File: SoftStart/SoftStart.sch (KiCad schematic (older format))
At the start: 26 parts, among them J1 LIVE, J10 LIVE, J2 NEUTRAL, J3 SW1, J4 SW2, J5 NEUTRAL, J6 SWOUTPUT, J7 LIVE, J8 LIVE, J9 LIVE

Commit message: Submitted to JLCPCB 2020-08-24
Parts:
- C1: LCSC (none) -> C342770
- C2: LCSC (none) -> C390065
- C3: LCSC (none) -> C338226
- D1, D2, D3, D4: LCSC (none) -> C193790
- D5: LCSC (none) -> C2552
- D6: LCSC (none) -> C99771
- R1: LCSC (none) -> C334296
- R2: LCSC (none) -> C58595
- R3, R4, R5, R6: value 220R -> 150R; LCSC (none) -> C334292
- RLY1: LCSC (none) -> C133339
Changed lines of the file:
@@
 F 2 "SoftStart:SMIHRelay" H 6550 2450 60  0001 C CNN
 F 3 "" H 6550 2450 60  0001 C CNN
+F 4 "C133339" H 6550 2450 60  0001 C CNN "LCSC"
 	1    6550 2450
 	1    0    0    -1
@@
 F 2 "Capacitors_THT:C_Rect_L11.5mm_W4.5mm_P10.00mm_MKT" H 2700 2600 50  0001 C CNN
 F 3 "" H 2700 2600 50  0001 C CNN
+F 4 " C342770" H 2700 2600 60  0001 C CNN "LCSC"
 	1    2700 2600
 	0    1    1    0
@@
 F 2 "Resistors_THT:R_Axial_Power_L20.0mm_W6.4mm_P22.40mm" V 3330 2600 50  0001 C CNN
 F 3 "" H 3400 2600 50  0001 C CNN
+F 4 "C334296" V 3400 2600 60  0001 C CNN "LCSC"
 	1    3400 2600
 	0    1    1    0
@@
 F 2 "Capacitors_THT:C_Rect_L24.0mm_W10.1mm_P22.50mm_MKT" H 3800 2600 50  0001 C CNN
 F 3 "" H 3800 2600 50  0001 C CNN
+F 4 "C390065" H 3800 2600 60  0001 C CNN "LCSC"
 	1    3800 2600
 	0    1    1    0
@@
 F 2 "Diodes_THT:D_DO-41_SOD81_P7.62mm_Horizontal" H 4100 2350 50  0001 C CNN
 F 3 "" H 4100 2350 50  0001 C CNN
+F 4 "C193790" H 4100 2350 60  0001 C CNN "LCSC"
 	1    4100 2350
 	0    1    1    0
@@
 F 2 "Diodes_THT:D_DO-41_SOD81_P7.62mm_Horizontal" H 4100 2850 50  0001 C CNN
 F 3 "" H 4100 2850 50  0001 C CNN
+F 4 "C193790" H 4100 2850 60  0001 C CNN "LCSC"
 	1    4100 2850
 	0    1    1    0
@@
 F 2 "Diodes_THT:D_DO-41_SOD81_P7.62mm_Horizontal" H 4500 2350 50  0001 C CNN
 F 3 "" H 4500 2350 50  0001 C CNN
+F 4 "C193790" H 4500 2350 60  0001 C CNN "LCSC"
 	1    4500 2350
 	0    1    1    0
@@
 F 2 "Diodes_THT:D_DO-41_SOD81_P7.62mm_Horizontal" H 4500 2850 50  0001 C CNN
 F 3 "" H 4500 2850 50  0001 C CNN
+F 4 "C193790" H 4500 2850 60  0001 C CNN "LCSC"
 	1    4500 2850
 	0    1    1    0
@@
 F 2 "Diodes_THT:D_DO-41_SOD81_P7.62mm_Horizontal" H 4900 2550 50  0001 C CNN
 F 3 "" H 4900 2550 50  0001 C CNN
+F 4 "C2552" H 4900 2550 60  0001 C CNN "LCSC"
 	1    4900 2550
 	0    1    1    0
@@
 F 2 "Capacitors_THT:CP_Radial_D10.0mm_P5.00mm" H 5250 2550 50  0001 C CNN
 F 3 "" H 5250 2550 50  0001 C CNN
+F 4 "C338226" H 5250 2550 60  0001 C CNN "LCSC"
 	1    5250 2550
 	1    0    0    -1
@@
 F 2 "LEDs:LED_D3.0mm" H 5650 2850 50  0001 C CNN
 F 3 "" H 5650 2850 50  0001 C CNN
+F 4 "C99771" H 5650 2850 60  0001 C CNN "LCSC"
 	1    5650 2850
 	0    -1   -1   0
@@
 F 2 "Resistors_THT:R_Axial_DIN0207_L6.3mm_D2.5mm_P7.62mm_Horizontal" V 5580 2400 50  0001 C CNN
 F 3 "" H 5650 2400 50  0001 C CNN
+F 4 "C58595" V 5650 2400 60  0001 C CNN "LCSC"
 	1    5650 2400
 	-1   0    0    1
@@
 P 7950 2250
 F 0 "R3" V 8030 2250 50  0000 C CNN
-F 1 "220R" V 7950 2250 50  0000 C CNN
+F 1 "150R" V 7950 2250 50  0000 C CNN
 F 2 "Resistors_THT:R_Axial_Power_L20.0mm_W6.4mm_P22.40mm" V 7880 2250 50  0001 C CNN
 F 3 "" H 7950 2250 50  0001 C CNN
+F 4 "C334292" V 7950 2250 60  0001 C CNN "LCSC"
 	1    7950 2250
 	-1   0    0    1
@@
 P 8350 2250
 F 0 "R4" V 8430 2250 50  0000 C CNN
-F 1 "220R" V 8350 2250 50  0000 C CNN
+F 1 "150R" V 8350 2250 50  0000 C CNN
 F 2 "Resistors_THT:R_Axial_Power_L20.0mm_W6.4mm_P22.40mm" V 8280 2250 50  0001 C CNN
 F 3 "" H 8350 2250 50  0001 C CNN
+F 4 "C334292" V 8350 2250 60  0001 C CNN "LCSC"
 	1    8350 2250
 	-1   0    0    1
@@
 P 8750 2250
 F 0 "R5" V 8830 2250 50  0000 C CNN
-F 1 "220R" V 8750 2250 50  0000 C CNN
+F 1 "150R" V 8750 2250 50  0000 C CNN
 F 2 "Resistors_THT:R_Axial_Power_L20.0mm_W6.4mm_P22.40mm" V 8680 2250 50  0001 C CNN
 F 3 "" H 8750 2250 50  0001 C CNN
+F 4 "C334292" V 8750 2250 60  0001 C CNN "LCSC"
 	1    8750 2250
 	-1   0    0    1
@@
 P 9150 2250
 F 0 "R6" V 9230 2250 50  0000 C CNN
-F 1 "220R" V 9150 2250 50  0000 C CNN
+F 1 "150R" V 9150 2250 50  0000 C CNN
 F 2 "Resistors_THT:R_Axial_Power_L20.0mm_W6.4mm_P22.40mm" V 9080 2250 50  0001 C CNN
 F 3 "" H 9150 2250 50  0001 C CNN
+F 4 "C334292" V 9150 2250 60  0001 C CNN "LCSC"
 	1    9150 2250
 	-1   0    0    1

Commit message: Fixed nasty bug in soft start
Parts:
- added R7: 1M, Resistors_THT:R_Axial_DIN0207_L6.3mm_D2.5mm_P7.62mm_Horizontal, symbol R
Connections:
- net at R3.2, R4.2, R5.2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: now also C1.1, J4.1 (Pin_1), R1.2; no longer C1.2, J1.1 (Pin_1), J3.1 (Pin_1)
- net at C2.2, R1.1: now also R7.2
- net at C2.1, D1.2 (A), D2.1 (K): now also R7.1
- new net: C1.2, J1.1 (Pin_1), J3.1 (Pin_1)
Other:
- moved on the sheet: C2, R1
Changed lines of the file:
@@
 L R R1
 U 1 1 5F41102F
-P 3400 2600
-F 0 "R1" V 3480 2600 50  0000 C CNN
-F 1 "220R" V 3400 2600 50  0000 C CNN
-F 2 "Resistors_THT:R_Axial_Power_L20.0mm_W6.4mm_P22.40mm" V 3330 2600 50  0001 C CNN
-F 3 "" H 3400 2600 50  0001 C CNN
-F 4 "C334296" V 3400 2600 60  0001 C CNN "LCSC"
-	1    3400 2600
+P 3300 2600
+F 0 "R1" V 3380 2600 50  0000 C CNN
+F 1 "220R" V 3300 2600 50  0000 C CNN
+F 2 "Resistors_THT:R_Axial_Power_L20.0mm_W6.4mm_P22.40mm" V 3230 2600 50  0001 C CNN
+F 3 "" H 3300 2600 50  0001 C CNN
+F 4 "C334296" V 3300 2600 60  0001 C CNN "LCSC"
+	1    3300 2600
 	0    1    1    0
 $EndComp
@@
 L C_Small C2
 U 1 1 5F4110A1
-P 3800 2600
-F 0 "C2" H 3810 2670 50  0000 L CNN
-F 1 "1 uF" H 3810 2520 50  0000 L CNN
-F 2 "Capacitors_THT:C_Rect_L24.0mm_W10.1mm_P22.50mm_MKT" H 3800 2600 50  0001 C CNN
-F 3 "" H 3800 2600 50  0001 C CNN
-F 4 "C390065" H 3800 2600 60  0001 C CNN "LCSC"
-	1    3800 2600
+P 3700 2600
+F 0 "C2" H 3710 2670 50  0000 L CNN
+F 1 "1 uF" H 3710 2520 50  0000 L CNN
+F 2 "Capacitors_THT:C_Rect_L24.0mm_W10.1mm_P22.50mm_MKT" H 3700 2600 50  0001 C CNN
+F 3 "" H 3700 2600 50  0001 C CNN
+F 4 "C390065" H 3700 2600 60  0001 C CNN "LCSC"
+	1    3700 2600
 	0    1    1    0
 $EndComp
@@
 	3000 2250 3000 2600
 Wire Wire Line
-	2800 2600 3250 2600
+	2800 2600 3150 2600
 Connection ~ 2400 2600
 Connection ~ 3000 2600
 Wire Wire Line
-	3700 2600 3550 2600
+	3600 2600 3450 2600
 Wire Wire Line
 	4100 2500 4100 2700
 Wire Wire Line
-	4100 2600 3900 2600
+	4100 2600 3800 2600
 Connection ~ 4100 2600
 Wire Wire Line
@@
 Connection ~ 5650 3100
 Wire Wire Line
-	2050 2600 2050 1600
-Wire Wire Line
-	2050 1600 9150 1600
+	3150 1600 9150 1600
 Wire Wire Line
 	7450 1600 7450 2450
 Wire Wire Line
 	7450 2450 7050 2450
-Connection ~ 2050 2600
 Wire Wire Line
 	5950 2350 5950 3600
@@
 $EndComp
 Connection ~ 7450 1600
+Wire Wire Line
+	3150 2600 3150 1600
+Connection ~ 3150 2600
+$Comp
+L R R7
+U 1 1 5F4604E8
+P 3700 2300
+F 0 "R7" V 3780 2300 50  0000 C CNN
+F 1 "1M" V 3700 2300 50  0000 C CNN
+F 2 "Resistors_THT:R_Axial_DIN0207_L6.3mm_D2.5mm_P7.62mm_Horizontal" V 3630 2300 50  0001 C CNN
+F 3 "" H 3700 2300 50  0001 C CNN
+F 4 "C334296" V 3700 2300 60  0001 C CNN "LCSC"
+	1    3700 2300
+	0    1    1    0
+$EndComp
+Wire Wire Line
+	3850 2300 3900 2300
+Wire Wire Line
+	3900 2300 3900 2600
+Connection ~ 3900 2600
+Wire Wire Line
+	3550 2300 3500 2300
+Wire Wire Line
+	3500 2300 3500 2600
+Connection ~ 3500 2600
 $EndSCHEMATC

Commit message: Changed softstart and Poweramp to TO-220 transistors
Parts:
- added D7, D8: 1N4742, Diodes_THT:D_DO-41_SOD81_P7.62mm_Horizontal, symbol D_Zener
- added J11: Conn_01x02, Connectors_Terminal_Blocks:TerminalBlock_bornier-2_P5.08mm, symbol Conn_01x02
- added RLY2: SPDTRelay, SoftStart:SMIHRelay, symbol SPDTRelay
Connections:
- net at C1.2, J1.1 (Pin_1), J3.1 (Pin_1): now also RLY2.3 (NO)
- net at C1.1, J4.1 (Pin_1), R1.2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: now also RLY2.1 (Pole)
- new net: D7.1 (K), J11.2 (Pin_2), RLY2.4 (Coil)
- new net: D8.1 (K), J11.1 (Pin_1), RLY2.5 (Coil)
- new net: D7.2 (A), D8.2 (A)
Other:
- moved on the sheet: C1, C2, C3, D1, D2, D3, D4, D5, D6, J1, J10, J2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

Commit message: Working design 2020-10-12
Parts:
- added J12, J13, J14, J15, J16, J17: NEUTRAL, Connectors:1pin, symbol Conn_01x01
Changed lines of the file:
@@
 	1600 2600 1600 2850
 Connection ~ 1850 2850
+$Comp
+L Conn_01x01 J12
+U 1 1 5F6D1F0A
+P 1350 4850
+F 0 "J12" H 1350 4950 50  0000 C CNN
+F 1 "NEUTRAL" H 1350 4750 50  0000 C CNN
+F 2 "Connectors:1pin" H 1350 4850 50  0001 C CNN
+F 3 "" H 1350 4850 50  0001 C CNN
+	1    1350 4850
+	-1   0    0    1
+$EndComp
+$Comp
+L Conn_01x01 J13
+U 1 1 5F6D1F9C
+P 1350 5150
+F 0 "J13" H 1350 5250 50  0000 C CNN
+F 1 "NEUTRAL" H 1350 5050 50  0000 C CNN
+F 2 "Connectors:1pin" H 1350 5150 50  0001 C CNN
+F 3 "" H 1350 5150 50  0001 C CNN
+	1    1350 5150
+	-1   0    0    1
+$EndComp
+$Comp
+L Conn_01x01 J15
+U 1 1 5F6D2021
+P 1900 4850
+F 0 "J15" H 1900 4950 50  0000 C CNN
+F 1 "NEUTRAL" H 1900 4750 50  0000 C CNN
+F 2 "Connectors:1pin" H 1900 4850 50  0001 C CNN
+F 3 "" H 1900 4850 50  0001 C CNN
+	1    1900 4850
+	-1   0    0    1
+$EndComp
+$Comp
+L Conn_01x01 J16
+U 1 1 5F6D20A5
+P 1900 5150
+F 0 "J16" H 1900 5250 50  0000 C CNN
+F 1 "NEUTRAL" H 1900 5050 50  0000 C CNN
+F 2 "Connectors:1pin" H 1900 5150 50  0001 C CNN
+F 3 "" H 1900 5150 50  0001 C CNN
+	1    1900 5150
+	-1   0    0    1
+$EndComp
+$Comp
+L Conn_01x01 J14
+U 1 1 5F6D214B
+P 1350 5550
+F 0 "J14" H 1350 5650 50  0000 C CNN
+F 1 "NEUTRAL" H 1350 5450 50  0000 C CNN
+F 2 "Connectors:1pin" H 1350 5550 50  0001 C CNN
+F 3 "" H 1350 5550 50  0001 C CNN
+	1    1350 5550
+	-1   0    0    1
+$EndComp
+$Comp
+L Conn_01x01 J17
+U 1 1 5F6D21D3
+P 1900 5550
+F 0 "J17" H 1900 5650 50  0000 C CNN
+F 1 "NEUTRAL" H 1900 5450 50  0000 C CNN
+F 2 "Connectors:1pin" H 1900 5550 50  0001 C CNN
+F 3 "" H 1900 5550 50  0001 C CNN
+	1    1900 5550
+	-1   0    0    1
+$EndComp
 $EndSCHEMATC

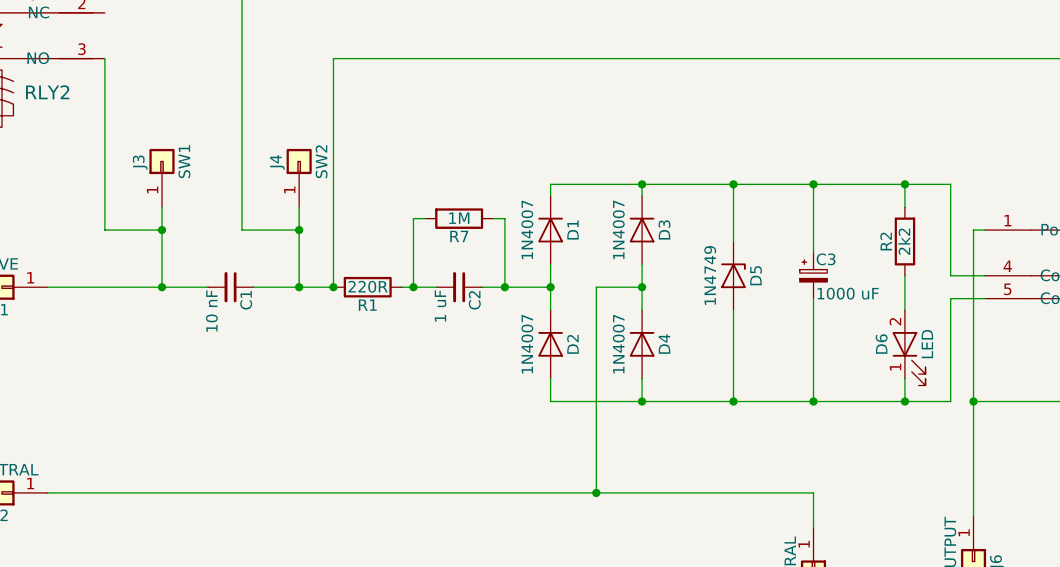
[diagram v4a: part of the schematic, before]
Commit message: Changed components for lower quiescent power
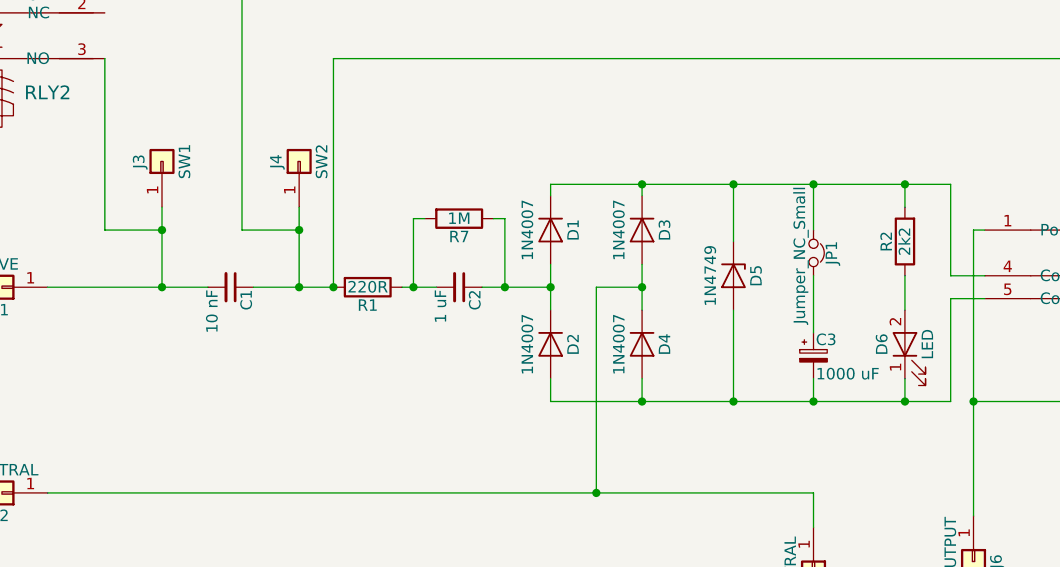
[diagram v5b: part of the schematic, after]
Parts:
- added JP1: Jumper_NC_Small, Pin_Headers:Pin_Header_Straight_1x02_Pitch2.54mm, symbol Jumper_NC_Small
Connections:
- net at D1.1 (K), D3.1 (K), D5.1 (K)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: now also JP1.1; no longer C3.1
- new net: C3.1, JP1.2
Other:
- moved on the sheet: C3
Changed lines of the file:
@@
 L CP_Small C3
 U 1 1 5F4113E8
-P 6650 3350
-F 0 "C3" H 6660 3420 50  0000 L CNN
-F 1 "1000 uF" H 6660 3270 50  0000 L CNN
-F 2 "Capacitors_THT:CP_Radial_D10.0mm_P5.00mm" H 6650 3350 50  0001 C CNN
-F 3 "" H 6650 3350 50  0001 C CNN
-F 4 "C338226" H 6650 3350 60  0001 C CNN "LCSC"
-	1    6650 3350
+P 6650 3700
+F 0 "C3" H 6660 3770 50  0000 L CNN
+F 1 "1000 uF" H 6660 3620 50  0000 L CNN
+F 2 "Capacitors_THT:CP_Radial_D10.0mm_P5.00mm" H 6650 3700 50  0001 C CNN
+F 3 "" H 6650 3700 50  0001 C CNN
+F 4 "C338226" H 6650 3700 60  0001 C CNN "LCSC"
+	1    6650 3700
 	1    0    0    -1
 $EndComp
@@
 	-1   0    0    1
 $EndComp
-Wire Wire Line
-	3800 3400 3800 3050
-Wire Wire Line
-	3300 3400 4000 3400
-Wire Wire Line
-	4400 3050 4400 3400
-Wire Wire Line
-	4200 3400 4550 3400
-Connection ~ 3800 3400
-Connection ~ 4400 3400
-Wire Wire Line
-	5000 3400 4850 3400
-Wire Wire Line
-	5500 3300 5500 3500
-Wire Wire Line
-	5500 3400 5200 3400
-Connection ~ 5500 3400
-Wire Wire Line
-	5900 3300 5900 3500
-Wire Wire Line
-	5900 3400 5700 3400
-Wire Wire Line
-	5700 3400 5700 4300
-Wire Wire Line
-	3300 4300 6650 4300
-Connection ~ 5900 3400
-Wire Wire Line
-	5900 3800 5900 3900
-Wire Wire Line
-	5500 3900 7250 3900
-Wire Wire Line
-	5500 3900 5500 3800
-Wire Wire Line
-	5500 3000 5500 2950
-Wire Wire Line
-	5500 2950 7250 2950
-Wire Wire Line
-	5900 2950 5900 3000
-Wire Wire Line
-	6300 2950 6300 3200
-Connection ~ 5900 2950
-Wire Wire Line
-	6300 3900 6300 3500
-Connection ~ 5900 3900
-Wire Wire Line
-	6650 2950 6650 3250
-Connection ~ 6300 2950
-Wire Wire Line
-	6650 3900 6650 3450
-Connection ~ 6300 3900
-Connection ~ 6650 2950
-Connection ~ 6650 3900
-Wire Wire Line
-	7050 3900 7050 3800
-Wire Wire Line
-	7050 3350 7050 3500
-Wire Wire Line
-	7050 2950 7050 3050
-Wire Wire Line
-	7400 3350 7250 3350
-Wire Wire Line
-	7250 3350 7250 2950
-Connection ~ 7050 2950
-Wire Wire Line
-	7400 3450 7250 3450
-Wire Wire Line
-	7250 3450 7250 3900
-Connection ~ 7050 3900
-Wire Wire Line
-	4550 2400 10550 2400
-Wire Wire Line
-	8850 2400 8850 3250
-Wire Wire Line
-	8850 3250 8450 3250
-Wire Wire Line
-	7350 3150 7350 4400
-Wire Wire Line
-	7350 3150 7400 3150
-Wire Wire Line
-	6650 4300 6650 4450
-Connection ~ 5700 4300
-Wire Wire Line
-	9350 2400 9350 2900
-Wire Wire Line
-	7350 3900 10550 3900
-Wire Wire Line
-	9350 3900 9350 3200
-Connection ~ 7350 3900
-Wire Wire Line
-	9750 2400 9750 2900
-Connection ~ 9350 2400
-Wire Wire Line
-	9750 3900 9750 3200
-Connection ~ 9350 3900
-Wire Wire Line
-	10150 2400 10150 2900
-Connection ~ 9750 2400
-Wire Wire Line
-	10150 3900 10150 3200
-Connection ~ 9750 3900
 $Comp
 L R R6
@@
 	-1   0    0    1
 $EndComp
-Wire Wire Line
-	10550 2400 10550 2900
-Connection ~ 10150 2400
-Wire Wire Line
-	10550 3900 10550 3200
-Connection ~ 10150 3900
 Text Notes 7800 6950 0    60   ~ 0
 Soft Start Circuit\nDrafted by D. Marks\nPCB CC-BY-SA 4.0
@@
 	-1   0    0    1
 $EndComp
-Connection ~ 8850 2400
-Wire Wire Line
-	4550 3400 4550 2400
-Connection ~ 4550 3400
 $Comp
 L R R7
@@
 	0    1    1    0
 $EndComp
-Wire Wire Line
-	5250 3100 5300 3100
-Wire Wire Line
-	5300 3100 5300 3400
-Connection ~ 5300 3400
-Wire Wire Line
-	4950 3100 4900 3100
-Wire Wire Line
-	4900 3100 4900 3400
-Connection ~ 4900 3400
 $Comp
 L SPDTRelay RLY2
@@
 	1    0    0    -1
 $EndComp
-Wire Wire Line
-	3550 2400 3550 3150
-Wire Wire Line
-	3550 3150 3800 3150
-Connection ~ 3800 3150
-Wire Wire Line
-	2500 2300 2500 2000
-Wire Wire Line
-	2500 2000 4150 2000
-Wire Wire Line
-	4150 2000 4150 3150
-Wire Wire Line
-	4150 3150 4400 3150
-Connection ~ 4400 3150
 $Comp
 L Conn_01x02 J11
@@
 	0    1    1    0
 $EndComp
-Wire Wire Line
-	1850 2500 1850 2550
-Wire Wire Line
-	1600 2200 2300 2200
-Wire Wire Line
-	2300 2200 2300 2500
-Wire Wire Line
-	2300 2500 2500 2500
-Wire Wire Line
-	2500 2600 2300 2600
-Wire Wire Line
-	2300 2600 2300 2850
-Wire Wire Line
-	2300 2850 1600 2850
-Wire Wire Line
-	1400 2500 1600 2500
-Wire Wire Line
-	1600 2500 1600 2200
-Connection ~ 1850 2200
-Wire Wire Line
-	1400 2600 1600 2600
-Wire Wire Line
-	1600 2600 1600 2850
-Connection ~ 1850 2850
 $Comp
 L Conn_01x01 J12
@@
 	-1   0    0    1
 $EndComp
+$Comp
+L Jumper_NC_Small JP1
+U 1 1 5F979283
+P 6650 3250
+F 0 "JP1" H 6650 3330 50  0000 C CNN
+F 1 "Jumper_NC_Small" H 6660 3190 50  0000 C CNN
+F 2 "Pin_Headers:Pin_Header_Straight_1x02_Pitch2.54mm" H 6650 3250 50  0001 C CNN
+F 3 "" H 6650 3250 50  0001 C CNN
+	1    6650 3250
+	0    1    1    0
+$EndComp
+Wire Wire Line
+	3800 3050 3800 3400
+Wire Wire Line
+	3300 3400 4000 3400
+Wire Wire Line
+	4400 3050 4400 3400
+Wire Wire Line
+	4200 3400 4550 3400
+Connection ~ 3800 3400
+Connection ~ 4400 3400
+Wire Wire Line
+	4850 3400 5000 3400
+Wire Wire Line
+	5500 3300 5500 3500
+Wire Wire Line
+	5200 3400 5500 3400
+Connection ~ 5500 3400
+Wire Wire Line
+	5900 3300 5900 3500
+Wire Wire Line
+	5900 3400 5700 3400
+Wire Wire Line
+	5700 3400 5700 4300
+Wire Wire Line
+	3300 4300 6650 4300
+Connection ~ 5900 3400
+Wire Wire Line
+	5900 3800 5900 3900
+Wire Wire Line
+	5500 3900 7250 3900
+Wire Wire Line
+	5500 3900 5500 3800
+Wire Wire Line
+	5500 3000 5500 2950
+Wire Wire Line
+	5500 2950 7250 2950
+Wire Wire Line
+	5900 2950 5900 3000
+Wire Wire Line
+	6300 2950 6300 3200
+Connection ~ 5900 2950
+Wire Wire Line
+	6300 3900 6300 3500
+Connection ~ 5900 3900
+Connection ~ 6300 2950
+Wire Wire Line
+	6650 3900 6650 3800
+Connection ~ 6300 3900
+Connection ~ 6650 2950
+Connection ~ 6650 3900
+Wire Wire Line
+	7050 3900 7050 3800
+Wire Wire Line
+	7050 3350 7050 3500
+Wire Wire Line
+	7050 2950 7050 3050
+Wire Wire Line
+	7400 3350 7250 3350
+Wire Wire Line
+	7250 3350 7250 2950
+Connection ~ 7050 2950
+Wire Wire Line
+	7400 3450 7250 3450
+Wire Wire Line
+	7250 3450 7250 3900
+Connection ~ 7050 3900
+Wire Wire Line
+	4550 2400 10550 2400
+Wire Wire Line
+	8850 2400 8850 3250
+Wire Wire Line
+	8850 3250 8450 3250
+Wire Wire Line
+	7350 3150 7350 4400
+Wire Wire Line
+	7350 3150 7400 3150
+Wire Wire Line
+	6650 4300 6650 4450
+Connection ~ 5700 4300
+Wire Wire Line
+	9350 2400 9350 2900
+Wire Wire Line
+	7350 3900 10550 3900
+Wire Wire Line
+	9350 3900 9350 3200
+Connection ~ 7350 3900
+Wire Wire Line
+	9750 2400 9750 2900
+Connection ~ 9350 2400
+Wire Wire Line
+	9750 3900 9750 3200
+Connection ~ 9350 3900
+Wire Wire Line
+	10150 2400 10150 2900
+Connection ~ 9750 2400
+Wire Wire Line
+	10150 3900 10150 3200
+Connection ~ 9750 3900
+Wire Wire Line
+	10550 2400 10550 2900
+Connection ~ 10150 2400
+Wire Wire Line
+	10550 3900 10550 3200
+Connection ~ 10150 3900
+Connection ~ 8850 2400
+Wire Wire Line
+	4550 3400 4550 2400
+Connection ~ 4550 3400
+Wire Wire Line
+	5250 3100 5300 3100
+Wire Wire Line
+	5300 3100 5300 3400
+Connection ~ 5300 3400
+Wire Wire Line
+	4950 3100 4900 3100
+Wire Wire Line
+	4900 3100 4900 3400
+Connection ~ 4900 3400
+Wire Wire Line
+	3550 2400 3550 3150
+Wire Wire Line
+	3550 3150 3800 3150
+Connection ~ 3800 3150
+Wire Wire Line
+	2500 2300 2500 2000
+Wire Wire Line
+	2500 2000 4150 2000
+Wire Wire Line
+	4150 2000 4150 3150
+Wire Wire Line
+	4150 3150 4400 3150
+Connection ~ 4400 3150
+Wire Wire Line
+	1850 2500 1850 2550
+Wire Wire Line
+	1600 2200 2300 2200
+Wire Wire Line
+	2300 2200 2300 2500
+Wire Wire Line
+	2300 2500 2500 2500
+Wire Wire Line
+	2500 2600 2300 2600
+Wire Wire Line
+	2300 2600 2300 2850
+Wire Wire Line
+	2300 2850 1600 2850
+Wire Wire Line
+	1400 2500 1600 2500
+Wire Wire Line
+	1600 2500 1600 2200
+Connection ~ 1850 2200
+Wire Wire Line
+	1400 2600 1600 2600
+Wire Wire Line
+	1600 2600 1600 2850
+Connection ~ 1850 2850
+Wire Wire Line
+	6650 3150 6650 2950
+Wire Wire Line
+	6650 3350 6650 3600
 $EndSCHEMATC
